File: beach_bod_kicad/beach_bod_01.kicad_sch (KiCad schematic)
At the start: 76 parts, among them J1 Conn_01x01, J2 Conn_01x03_Male, J3 BNC5-J-P-GN-RA-BH2D, J4 Conn_01x01, J5 USB4085-GF-A_REVA4, J6 USB4085-GF-A_REVA4, Q1 AO3401A, U1 LTC6269, U2 LTC6268, U3 LM7301

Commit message: Layout Adjustments
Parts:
- removed C10, C15: CTRIM, Capacitor_SMD:C_Trimmer_Voltronics_JQ, symbol dad_bob-rescue:CTRIM-Device
- removed C11: 86nF, Capacitor_SMD:C_1210_3225Metric_Pad1.33x2.70mm_HandSolder, symbol Device:C
- removed J2: Conn_01x03_Male, Connector_PinHeader_2.54mm:PinHeader_1x03_P2.54mm_Vertical, symbol Connector:Conn_01x03_Male
- removed R10: 30M, Resistor_SMD:R_0805_2012Metric_Pad1.20x1.40mm_HandSolder, symbol Device:R
- C30, C31, C32, C33, C34: footprint Capacitor_SMD:C_0805_2012Metric_Pad1.18x1.45mm_HandSolder -> Capacitor_SMD:C_1210_3225Metric_Pad1.33x2.70mm_HandSolder
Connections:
- net at J1.1 (Pin_1): now also C2.2, R3.1
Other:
- moved on the sheet: R9

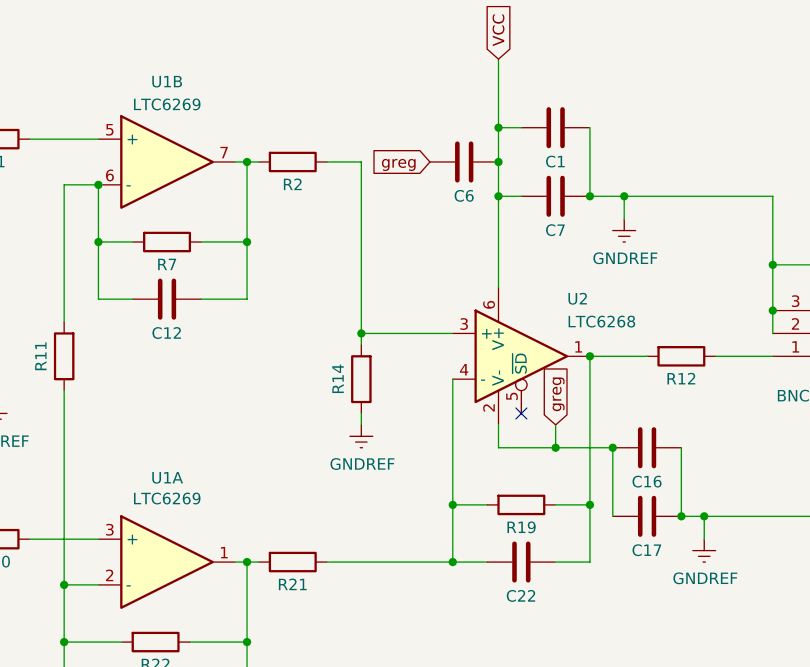
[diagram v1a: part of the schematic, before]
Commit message: Reworked ground plane & output opamp
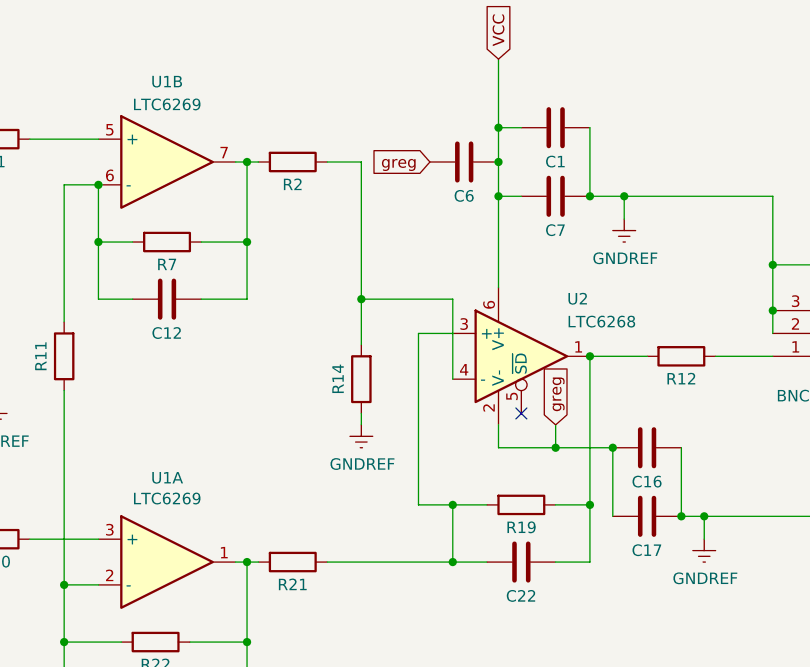
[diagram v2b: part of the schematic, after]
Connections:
- net at C22.2, R19.2, R21.1: now also U2.3 (+); no longer U2.4 (-)
- net at R14.2, R2.1: now also U2.4 (-); no longer U2.3 (+)
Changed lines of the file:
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@@
 (kicad_sch (version 20211123) (generator eeschema)
   (paper "A4")
-  (junction (at 191.135 67.945) (diameter 0) (color 0 0 0 0)
-  )
   (junction (at 67.945 80.645) (diameter 0) (color 0 0 0 0)
   )
@@
   (junction (at 69.215 168.275) (diameter 0) (color 0 0 0 0)
   )
+  (junction (at 201.295 86.995) (diameter 0) (color 0 0 0 0)
+  )
   (junction (at 94.615 191.135) (diameter 0) (color 0 0 0 0)
   )
@@
   (junction (at 94.615 163.195) (diameter 0) (color 0 0 0 0)
   )
+  (junction (at 191.135 64.135) (diameter 0) (color 0 0 0 0)
+  )
   (junction (at 178.435 48.895) (diameter 0) (color 0 0 0 0)
   )
@@
   )
   (junction (at 109.855 80.645) (diameter 0) (color 0 0 0 0)
-  )
-  (junction (at 201.295 86.995) (diameter 0) (color 0 0 0 0)
   )
   (junction (at 158.115 95.885) (diameter 0) (color 0 0 0 0)
@@
   (no_connect (at 217.805 145.415))
   (no_connect (at 208.915 76.835))
+  (wire (pts (xy 197.485 67.945) (xy 201.295 67.945))
+    (stroke (width 0) (type default) (color 0 0 0 0))
+  )
   (wire (pts (xy 64.135 168.275) (xy 69.215 168.275))
     (stroke (width 0) (type default) (color 0 0 0 0))
@@
     (stroke (width 0) (type default) (color 0 0 0 0))
   )
-  (wire (pts (xy 201.295 73.025) (xy 201.295 86.995))
-    (stroke (width 0) (type default) (color 0 0 0 0))
-  )
   (wire (pts (xy 236.855 65.405) (xy 236.855 60.325))
     (stroke (width 0) (type default) (color 0 0 0 0))
@@
     (stroke (width 0) (type default) (color 0 0 0 0))
   )
-  (wire (pts (xy 191.135 67.945) (xy 191.135 69.215))
-    (stroke (width 0) (type default) (color 0 0 0 0))
-  )
   (wire (pts (xy 177.165 48.895) (xy 178.435 48.895))
     (stroke (width 0) (type default) (color 0 0 0 0))
@@
     (stroke (width 0) (type default) (color 0 0 0 0))
   )
+  (wire (pts (xy 191.135 64.135) (xy 191.135 69.215))
+    (stroke (width 0) (type default) (color 0 0 0 0))
+  )
+  (wire (pts (xy 197.485 86.995) (xy 197.485 67.945))
+    (stroke (width 0) (type default) (color 0 0 0 0))
+  )
   (wire (pts (xy 217.805 153.035) (xy 217.805 155.575))
     (stroke (width 0) (type default) (color 0 0 0 0))
@@
     (stroke (width 0) (type default) (color 0 0 0 0))
   )
+  (wire (pts (xy 191.135 64.135) (xy 201.295 64.135))
+    (stroke (width 0) (type default) (color 0 0 0 0))
+  )
   (wire (pts (xy 109.855 67.945) (xy 109.855 69.215))
     (stroke (width 0) (type default) (color 0 0 0 0))
@@
     (stroke (width 0) (type default) (color 0 0 0 0))
   )
+  (wire (pts (xy 201.295 64.135) (xy 201.295 73.025))
+    (stroke (width 0) (type default) (color 0 0 0 0))
+  )
   (wire (pts (xy 94.615 168.275) (xy 94.615 174.625))
     (stroke (width 0) (type default) (color 0 0 0 0))
   )
-  (wire (pts (xy 201.295 67.945) (xy 191.135 67.945))
-    (stroke (width 0) (type default) (color 0 0 0 0))
-  )
   (wire (pts (xy 65.405 75.565) (xy 65.405 80.645))
     (stroke (width 0) (type default) (color 0 0 0 0))
@@
     (stroke (width 0) (type default) (color 0 0 0 0))
   )
+  (wire (pts (xy 201.295 86.995) (xy 197.485 86.995))
+    (stroke (width 0) (type default) (color 0 0 0 0))
+  )
   (wire (pts (xy 150.495 75.565) (xy 150.495 67.945))
     (stroke (width 0) (type default) (color 0 0 0 0))
@@
     (stroke (width 0) (type default) (color 0 0 0 0))
   )
-  (wire (pts (xy 191.135 48.895) (xy 191.135 67.945))
-    (stroke (width 0) (type default) (color 0 0 0 0))
-  )
+  (wire (pts (xy 191.135 48.895) (xy 191.135 64.135))
+    (stroke (width 0) (type default) (color 0 0 0 0))
+  )

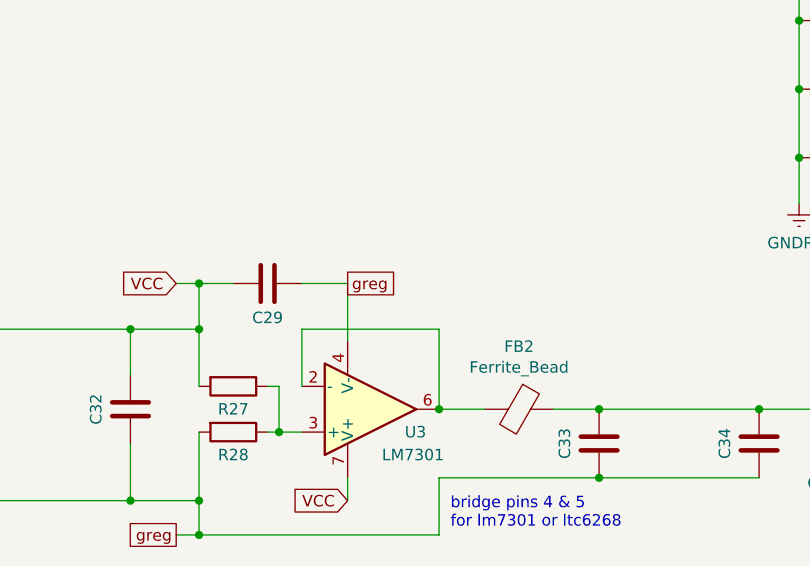
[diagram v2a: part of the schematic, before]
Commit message: Added buds_diffprobe_spice and waveforms psu testing
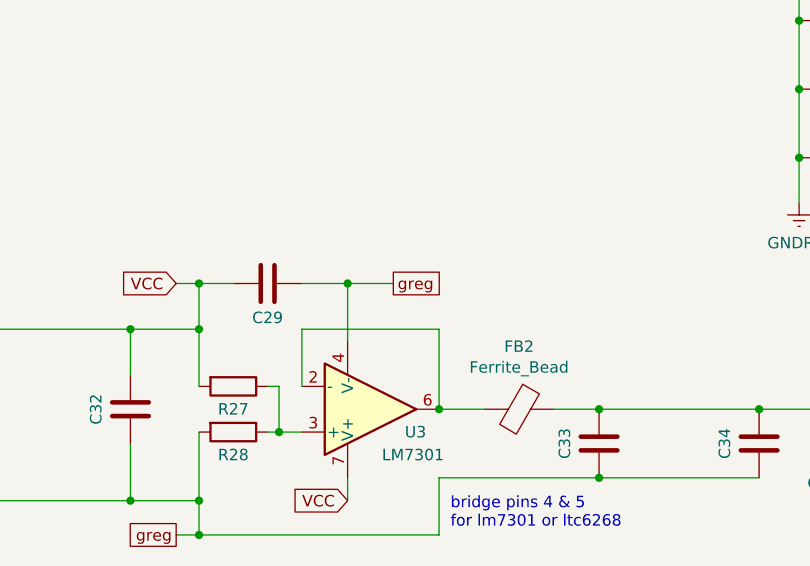
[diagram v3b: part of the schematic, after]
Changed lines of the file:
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@@
   (junction (at 86.995 168.275) (diameter 0) (color 0 0 0 0)
+  )
+  (junction (at 111.125 163.195) (diameter 0) (color 0 0 0 0)
   )
   (junction (at 109.855 80.645) (diameter 0) (color 0 0 0 0)
@@
     (stroke (width 0) (type default) (color 0 0 0 0))
   )
+  (wire (pts (xy 106.045 163.195) (xy 111.125 163.195))
+    (stroke (width 0) (type default) (color 0 0 0 0))
+  )
   (wire (pts (xy 217.805 153.035) (xy 217.805 155.575))
     (stroke (width 0) (type default) (color 0 0 0 0))
@@
     (stroke (width 0) (type default) (color 0 0 0 0))
   )
-  (wire (pts (xy 106.045 163.195) (xy 111.125 163.195))
-    (stroke (width 0) (type default) (color 0 0 0 0))
-  )
   (wire (pts (xy 94.615 163.195) (xy 94.615 168.275))
     (stroke (width 0) (type default) (color 0 0 0 0))
@@
   )
   (wire (pts (xy 150.495 67.945) (xy 141.605 67.945))
+    (stroke (width 0) (type default) (color 0 0 0 0))
+  )
+  (wire (pts (xy 111.125 163.195) (xy 116.205 163.195))
     (stroke (width 0) (type default) (color 0 0 0 0))
   )
@@
     )
   )
-  (global_label "greg" (shape passive) (at 111.125 163.195 0) (fields_autoplaced)
+  (global_label "greg" (shape passive) (at 116.205 163.195 0) (fields_autoplaced)
     (effects (font (size 1.27 1.27)) (justify left))
-    (property "Intersheet References" "${INTERSHEET_REFS}" (id 0) (at 0.635 4.445 0)
-      (effects (font (size 1.27 1.27)) hide)
-    )
+    (property "Intersheet References" "${INTERSHEET_REFS}" (id 0) (at 5.715 4.445 0)
+      (effects (font (size 1.27 1.27)) hide)
+    )
